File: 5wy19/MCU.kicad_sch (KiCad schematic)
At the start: 5 parts

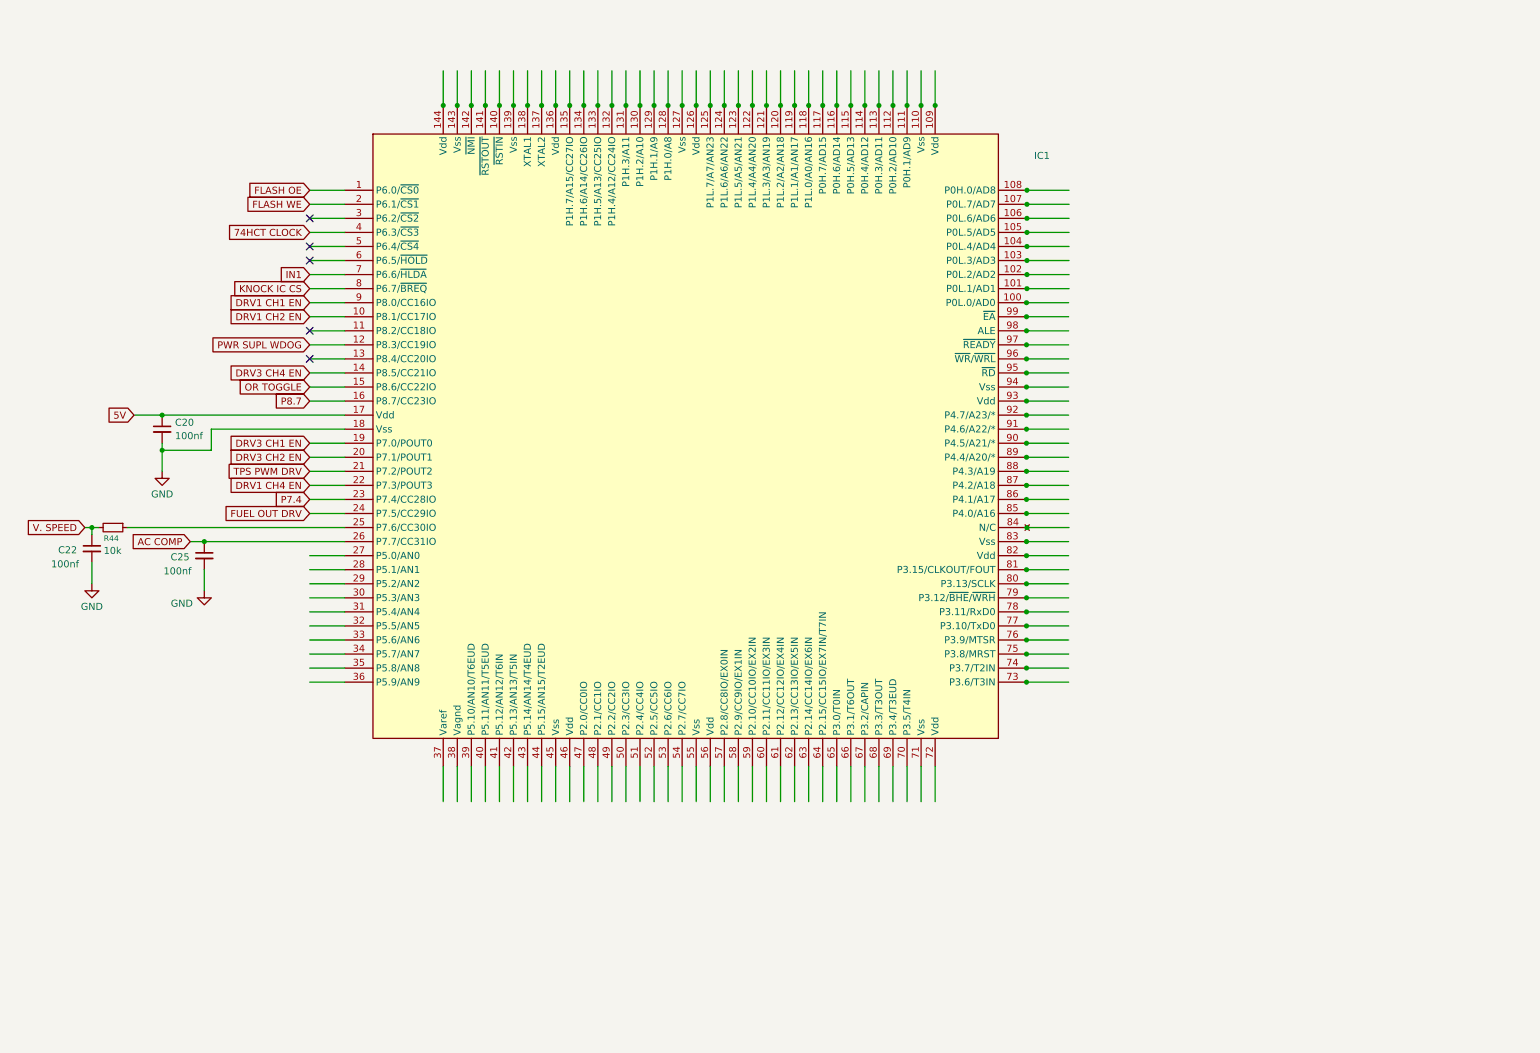
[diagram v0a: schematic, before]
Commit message: Further progress on MCU and connected circuits
Mostly sensors, knock control, some pins from the IO drivers and the unknown AMIS chip
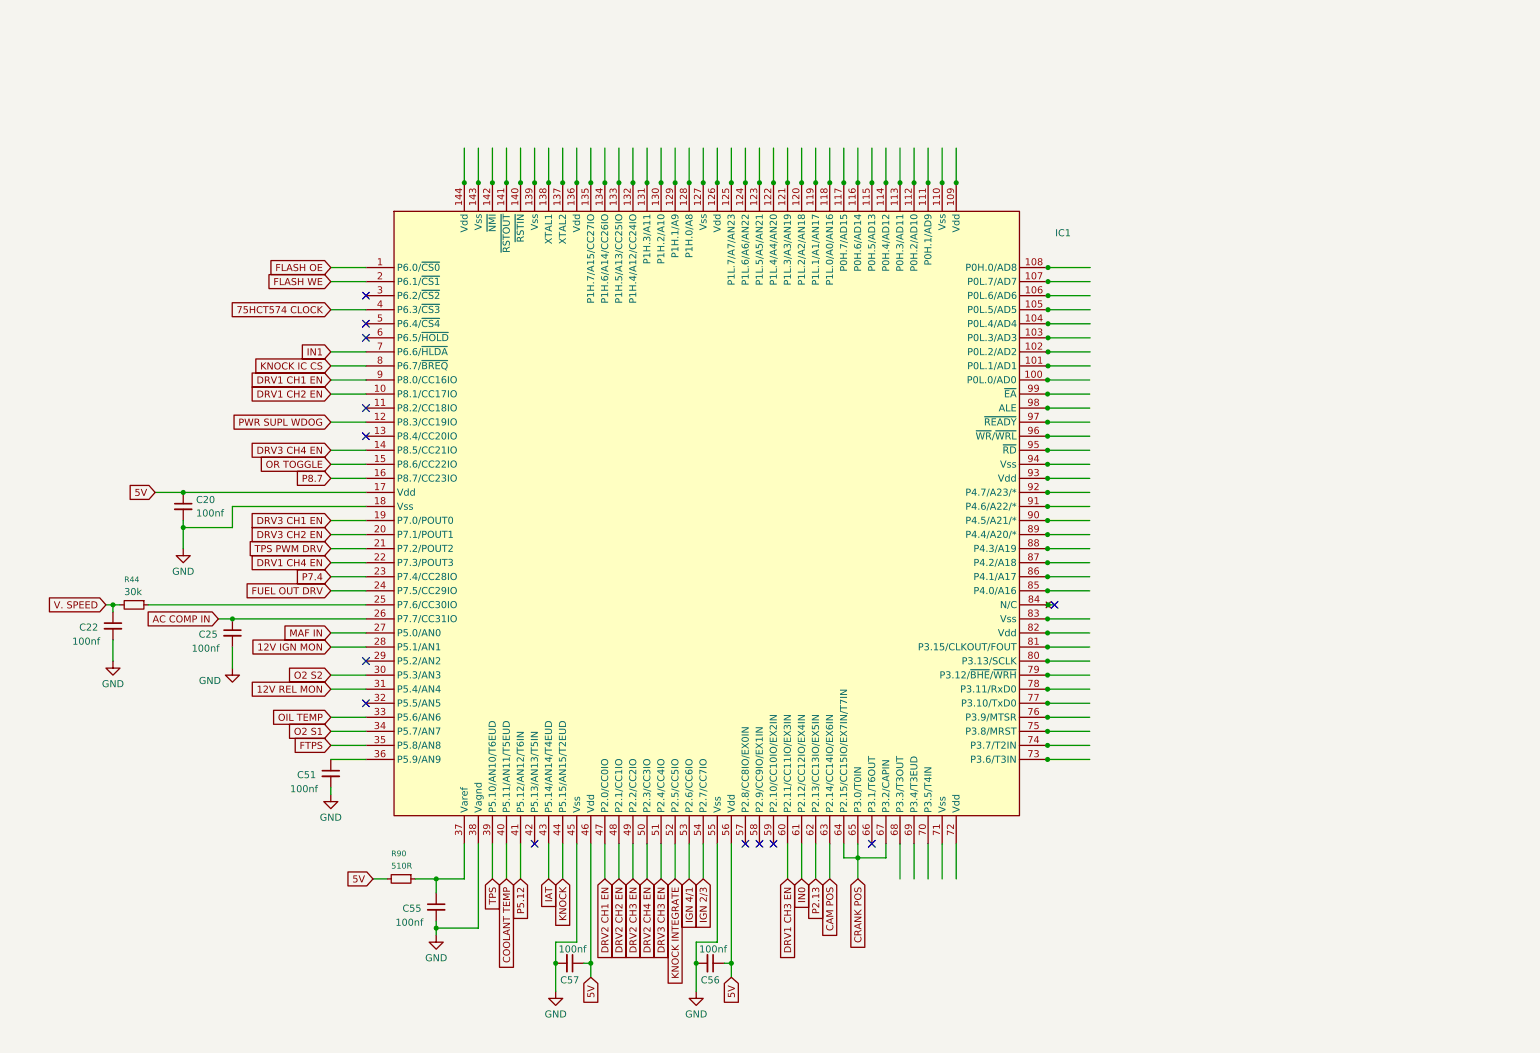
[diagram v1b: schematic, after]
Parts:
- added C51, C55, C56, C57: 100nf, symbol Device:C_Small
- added R90: 510R, symbol Device:R_Small
- R44: value 10k -> 30k
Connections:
- net 5V: now also IC1.46 (Vdd), IC1.56 (Vdd), C56.1, C57.1, R90.2
- net GND: now also IC1.38 (Vagnd), IC1.45 (Vss), IC1.55 (Vss), C51.2, C55.2, C56.2, C57.2
- net MAF IN: now reaches IC1.27 (P5.0/AN0)
- net 12V IGN MON: now reaches IC1.28 (P5.1/AN1)
- net O2 S2: now reaches IC1.30 (P5.3/AN3)
- net 12V REL MON: now reaches IC1.31 (P5.4/AN4)
- net OIL TEMP: now reaches IC1.33 (P5.6/AN6)
- net O2 S1: now reaches IC1.34 (P5.7/AN7)
- net FTPS: now reaches IC1.35 (P5.8/AN8)
- net at IC1.36 (P5.9/AN9): now also C51.1
- net at IC1.37 (Varef): now also C55.1, R90.1
- net TPS: now reaches IC1.39 (P5.10/AN10/T6EUD)
- net COOLANT TEMP: now reaches IC1.40 (P5.11/AN11/T5EUD)
- net P5.12: now reaches IC1.41 (P5.12/AN12/T6IN)
- net IAT: now reaches IC1.43 (P5.14/AN14/T4EUD)
- net KNOCK: now reaches IC1.44 (P5.15/AN15/T2EUD)
- net DRV2 CH1 EN: now reaches IC1.47 (P2.0/CC0IO)
- net DRV2 CH2 EN: now reaches IC1.48 (P2.1/CC1IO)
- net DRV2 CH3 EN: now reaches IC1.49 (P2.2/CC2IO)
- net DRV2 CH4 EN: now reaches IC1.50 (P2.3/CC3IO)
- net DRV3 CH3 EN: now reaches IC1.51 (P2.4/CC4IO)
- net KNOCK INTEGRATE: now reaches IC1.52 (P2.5/CC5IO)
- net IGN 4/1: now reaches IC1.53 (P2.6/CC6IO)
- net IGN 2/3: now reaches IC1.54 (P2.7/CC7IO)
- net DRV1 CH3 EN: now reaches IC1.60 (P2.11/CC11IO/EX3IN)
- net IN0: now reaches IC1.61 (P2.12/CC12IO/EX4IN)
- net P2.13: now reaches IC1.62 (P2.13/CC13IO/EX5IN)
- net CAM POS: now reaches IC1.63 (P2.14/CC14IO/EX6IN)
- net CRANK POS: now reaches IC1.64 (P2.15/CC15IO/EX7IN/T7IN)
- net CRANK POS: now also IC1.65 (P3.0/T0IN), IC1.67 (P3.2/CAPIN)
- net 74HCT CLOCK renamed 75HCT574 CLOCK
- net AC COMP renamed AC COMP IN
- no-connect marks 5 -> 13
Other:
- moved on the sheet: C20, C22, C25, IC1, R44

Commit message: Mapped out more pins of MCU and relevant circuits
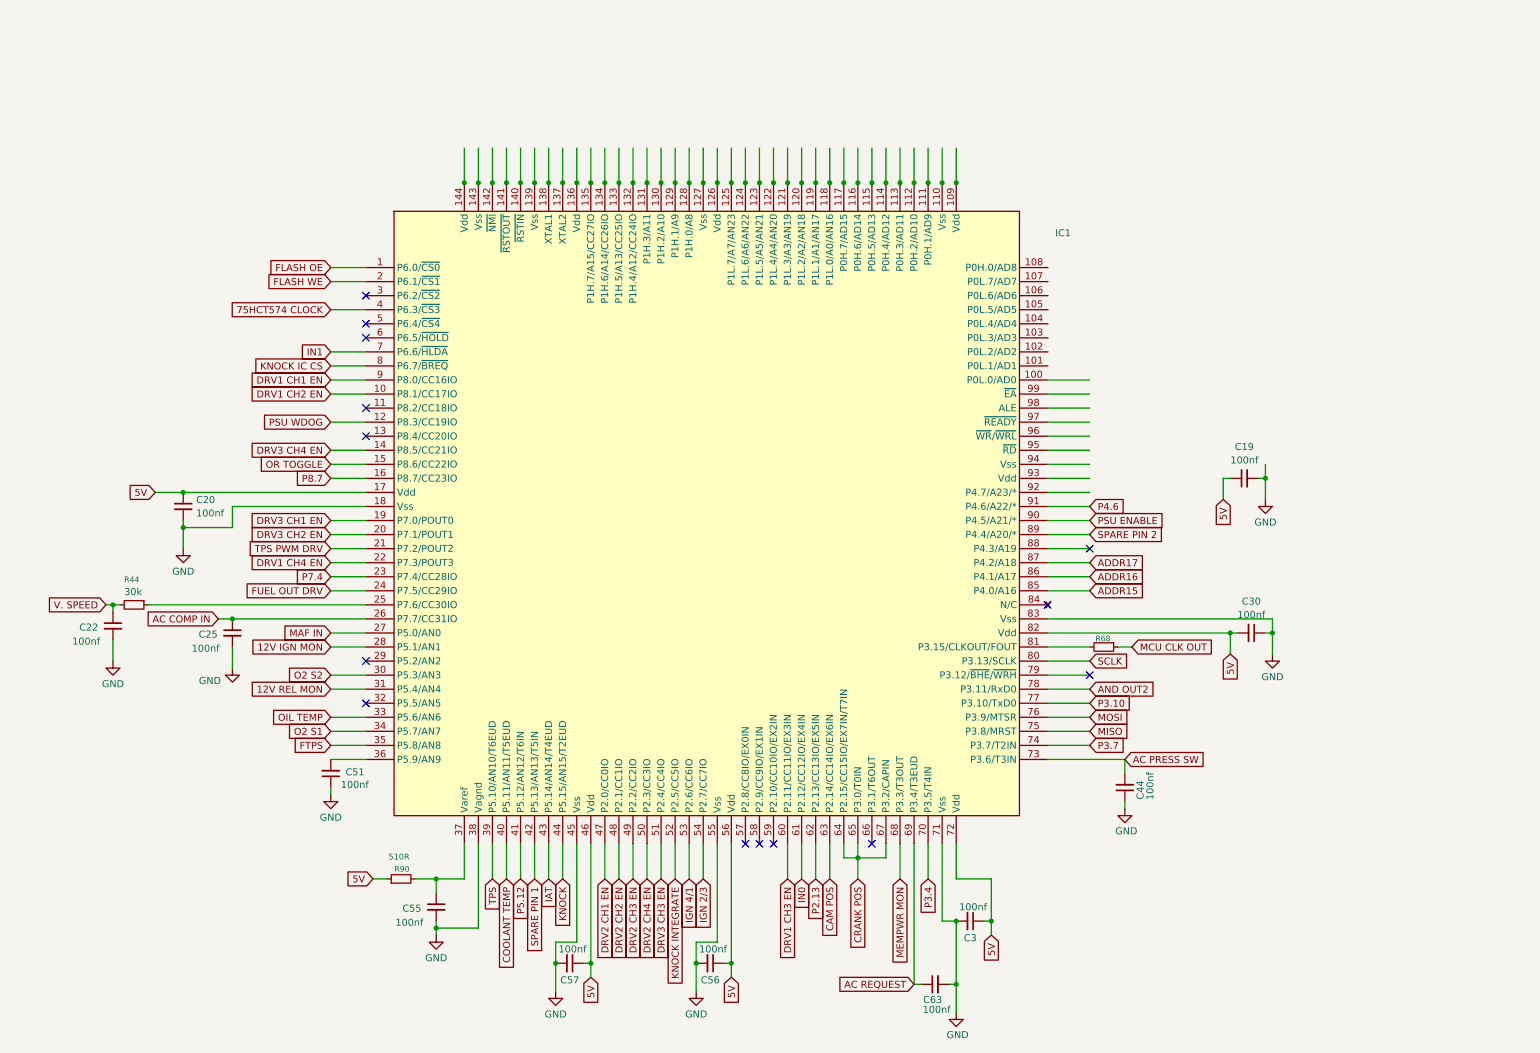
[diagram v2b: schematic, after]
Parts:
- added C19, C3, C30, C44, C63: 100nf, symbol Device:C_Small
- added R68: 100R, symbol Device:R_Small
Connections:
- net 5V: now also IC1.72 (Vdd), IC1.82 (Vdd), R90.1, C19.1, C3.1, C30.2; no longer R90.2
- net GND: now also C51.1, IC1.71 (Vss), IC1.83 (Vss), C19.2, C3.2, C30.1, C44.1, C63.2; no longer C51.2
- net at C55.1, IC1.37 (Varef): now also R90.2; no longer R90.1
- net at IC1.36 (P5.9/AN9): now also C51.2; no longer C51.1
- net SPARE PIN 1: now reaches IC1.42 (P5.13/AN13/T5IN)
- net MEMPWR MON: now reaches IC1.68 (P3.3/T3OUT)
- net AC REQUEST: now reaches IC1.69 (P3.4/T3EUD)
- net AC REQUEST: now also C63.1
- net P3.4: now reaches IC1.70 (P3.5/T4IN)
- net AC PRESS SW: now reaches IC1.73 (P3.6/T3IN)
- net AC PRESS SW: now also C44.2
- net P3.7: now reaches IC1.74 (P3.7/T2IN)
- net MISO: now reaches IC1.75 (P3.8/MRST)
- net MOSI: now reaches IC1.76 (P3.9/MTSR)
- net P3.10: now reaches IC1.77 (P3.10/TxD0)
- net AND OUT2: now reaches IC1.78 (P3.11/RxD0)
- net SCLK: now reaches IC1.80 (P3.13/SCLK)
- net at IC1.81 (P3.15/CLKOUT/FOUT): now also R68.2
- net ADDR15: now reaches IC1.85 (P4.0/A16)
- net ADDR16: now reaches IC1.86 (P4.1/A17)
- net ADDR17: now reaches IC1.87 (P4.2/A18)
- net SPARE PIN 2: now reaches IC1.89 (P4.4/A20/*)
- net PSU ENABLE: now reaches IC1.90 (P4.5/A21/*)
- net P4.6: now reaches IC1.91 (P4.6/A22/*)
- net PWR SUPL WDOG renamed PSU WDOG
- new net MCU CLK OUT: R68.1
- no-connect marks 13 -> 14
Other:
- moved on the sheet: C51, R90

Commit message: Finished most of the subsystems
-- MCU finished
-- Flash finished
-- Power Supply finished
-- I/O Drivers finished
-- CANBUS finished
-- Knock Control finished
-- Connector finished
-- Ignition Driver finished
-- Sensor Logic mostly finished
-- Logic ICs need some work
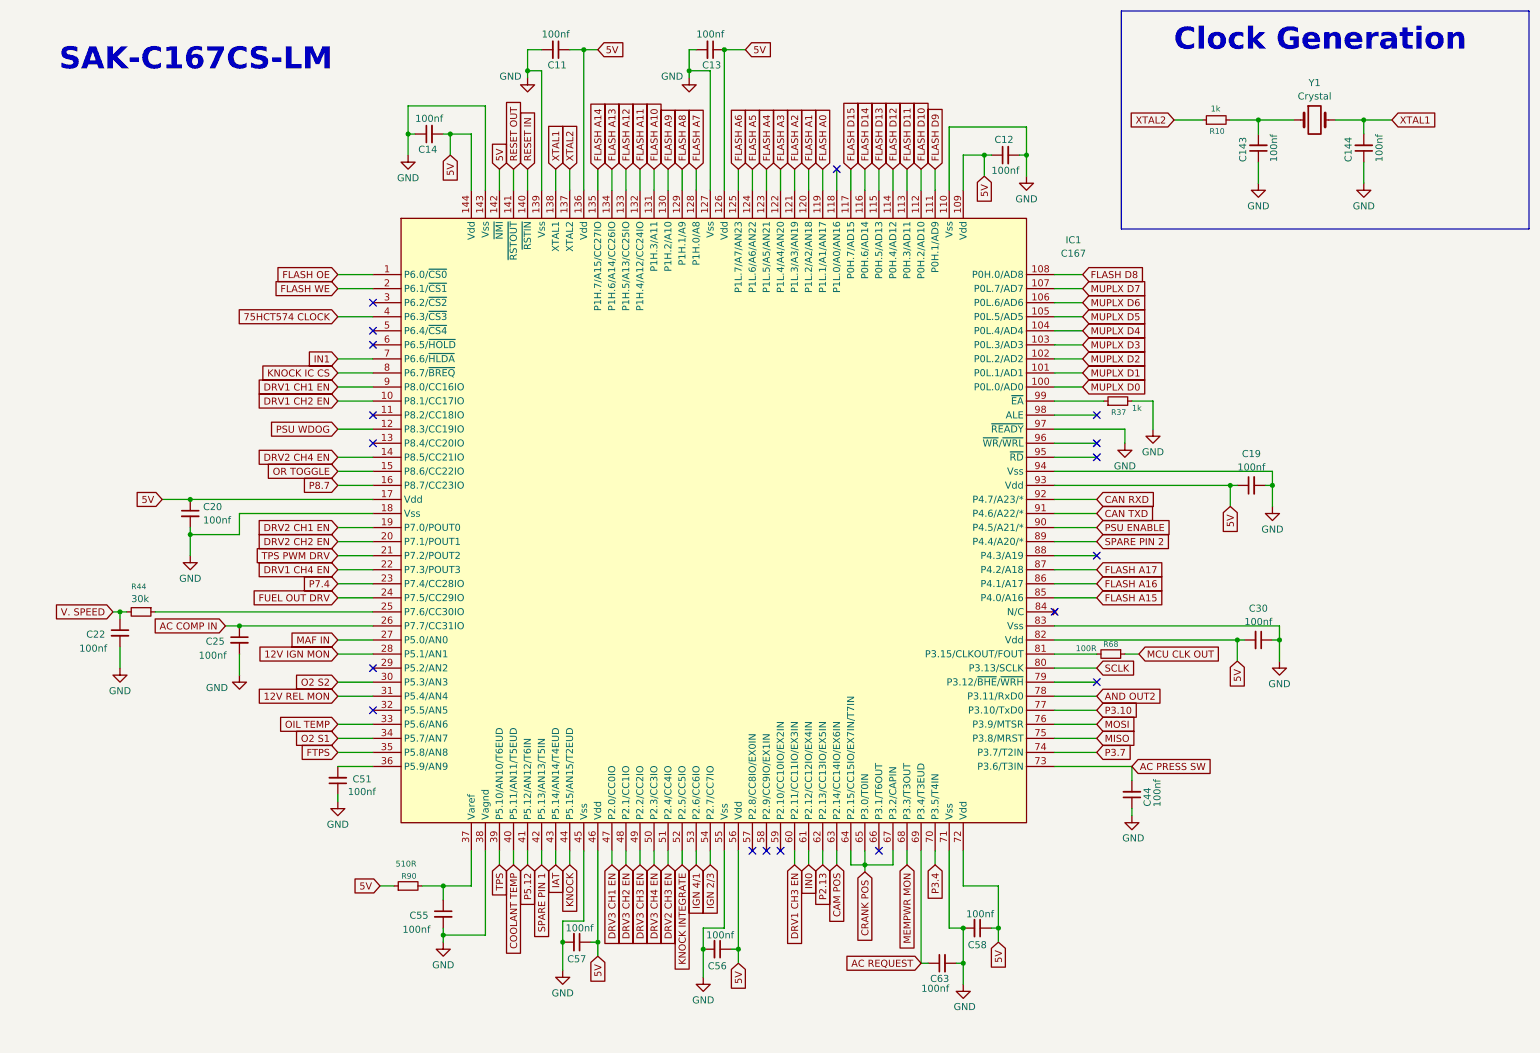
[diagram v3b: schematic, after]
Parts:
- added C11, C12, C13, C14, C143, C144: 100nf, symbol Device:C_Small
- added R10, R37: 1k, symbol Device:R_Small
- added Y1: Crystal, symbol Device:Crystal
- IC1: value ~ -> C167
- renumbered C3 to C58
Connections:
- net 5V: now also IC1.109 (Vdd), IC1.126 (Vdd), IC1.136 (Vdd), IC1.142 (~{NMI}), IC1.144 (Vdd), IC1.93 (Vdd), C11.1, C12.1, C13.1, C14.2
- net DRV2 CH1 EN: now also IC1.19 (P7.0/POUT0); no longer IC1.47 (P2.0/CC0IO)
- net DRV2 CH2 EN: now also IC1.20 (P7.1/POUT1); no longer IC1.48 (P2.1/CC1IO)
- net DRV2 CH3 EN: now also IC1.51 (P2.4/CC4IO); no longer IC1.49 (P2.2/CC2IO)
- net DRV2 CH4 EN: now also IC1.14 (P8.5/CC21IO); no longer IC1.50 (P2.3/CC3IO)
- net DRV3 CH1 EN: now also IC1.47 (P2.0/CC0IO); no longer IC1.19 (P7.0/POUT0)
- net DRV3 CH2 EN: now also IC1.48 (P2.1/CC1IO); no longer IC1.20 (P7.1/POUT1)
- net DRV3 CH3 EN: now also IC1.49 (P2.2/CC2IO); no longer IC1.51 (P2.4/CC4IO)
- net DRV3 CH4 EN: now also IC1.50 (P2.3/CC3IO); no longer IC1.14 (P8.5/CC21IO)
- net GND: now also IC1.110 (Vss), IC1.127 (Vss), IC1.139 (Vss), IC1.143 (Vss), IC1.94 (Vss), IC1.97 (~{READY}), C11.2, C12.2, C13.2, C14.1, C143.1, C144.1, R37.2
- net MUPLX D0: now reaches IC1.100 (P0L.0/AD0)
- net MUPLX D1: now reaches IC1.101 (P0L.1/AD1)
- net MUPLX D2: now reaches IC1.102 (P0L.2/AD2)
- net MUPLX D3: now reaches IC1.103 (P0L.3/AD3)
- net MUPLX D4: now reaches IC1.104 (P0L.4/AD4)
- net MUPLX D5: now reaches IC1.105 (P0L.5/AD5)
- net MUPLX D6: now reaches IC1.106 (P0L.6/AD6)
- net MUPLX D7: now reaches IC1.107 (P0L.7/AD7)
- net FLASH D8: now reaches IC1.108 (P0H.0/AD8)
- net FLASH D9: now reaches IC1.111 (P0H.1/AD9)
- net FLASH D10: now reaches IC1.112 (P0H.2/AD10)
- net FLASH D11: now reaches IC1.113 (P0H.3/AD11)
- net FLASH D12: now reaches IC1.114 (P0H.4/AD12)
- net FLASH D13: now reaches IC1.115 (P0H.5/AD13)
- net FLASH D14: now reaches IC1.116 (P0H.6/AD14)
- net FLASH D15: now reaches IC1.117 (P0H.7/AD15)
- net FLASH A0: now reaches IC1.119 (P1L.1/A1/AN17)
- net FLASH A1: now reaches IC1.120 (P1L.2/A2/AN18)
- net FLASH A2: now reaches IC1.121 (P1L.3/A3/AN19)
- net FLASH A3: now reaches IC1.122 (P1L.4/A4/AN20)
- net FLASH A4: now reaches IC1.123 (P1L.5/A5/AN21)
- net FLASH A5: now reaches IC1.124 (P1L.6/A6/AN22)
- net FLASH A6: now reaches IC1.125 (P1L.7/A7/AN23)
- net FLASH A7: now reaches IC1.128 (P1H.0/A8)
- net FLASH A8: now reaches IC1.129 (P1H.1/A9)
- net FLASH A9: now reaches IC1.130 (P1H.2/A10)
- net FLASH A10: now reaches IC1.131 (P1H.3/A11)
- net FLASH A11: now reaches IC1.132 (P1H.4/A12/CC24IO)
- net FLASH A12: now reaches IC1.133 (P1H.5/A13/CC25IO)
- net FLASH A13: now reaches IC1.134 (P1H.6/A14/CC26IO)
- net FLASH A14: now reaches IC1.135 (P1H.7/A15/CC27IO)
- net XTAL2: now reaches IC1.137 (XTAL2)
- net XTAL2: now also R10.1
- net XTAL1: now reaches IC1.138 (XTAL1)
- net XTAL1: now also C144.2, Y1.2
- net RESET IN: now reaches IC1.140 (~{RSTIN})
- net RESET OUT: now reaches IC1.141 (~{RSTOUT})
- net CAN RXD: now reaches IC1.92 (P4.7/A23/*)
- net at IC1.99 (~{EA}): now also R37.1
- net ADDR15 renamed FLASH A15
- net ADDR16 renamed FLASH A16
- net ADDR17 renamed FLASH A17
- net P4.6 renamed CAN TXD
- new net: C143.2, R10.2, Y1.1
- no-connect marks 14 -> 18
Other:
- note added: "Clock Generation"
- note added: "SAK-C167CS-LM"
- title: (none) -> SMIK43 5WY19 Rev. Eng
- moved on the sheet: C19, C20, C22, C25, C30, C44, C51, C55, C56, C57, C58, C63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

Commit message: Final schematic (except maybe some oversights)
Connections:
- net V. SPEED: no longer C22.1
- net XTAL1: now also Y1.1; no longer Y1.2
- net at C143.2, R10.2: now also Y1.2; no longer Y1.1
- net at IC1.25 (P7.6/CC30IO), R44.1: now also C22.1
- net AND OUT2 renamed RxD
- net MUPLX D0 renamed MLTPLX D0
- net MUPLX D1 renamed MLTPLX D1
- net MUPLX D2 renamed MLTPLX D2
- net MUPLX D3 renamed MLTPLX D3
- net MUPLX D4 renamed MLTPLX D4
- net MUPLX D5 renamed MLTPLX D5
- net MUPLX D6 renamed MLTPLX D6
- net MUPLX D7 renamed MLTPLX D7
- net P3.10 renamed TxD
- net P7.4 renamed RxD Out 2
- net P8.7 renamed RxD Out 1
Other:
- moved on the sheet: C22, C44, R44, Y1
